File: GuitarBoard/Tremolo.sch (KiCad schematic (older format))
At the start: 37 parts, among them Q2 2N5088, Q7 2N5088, Q8 2N5088, Q9 2N5088

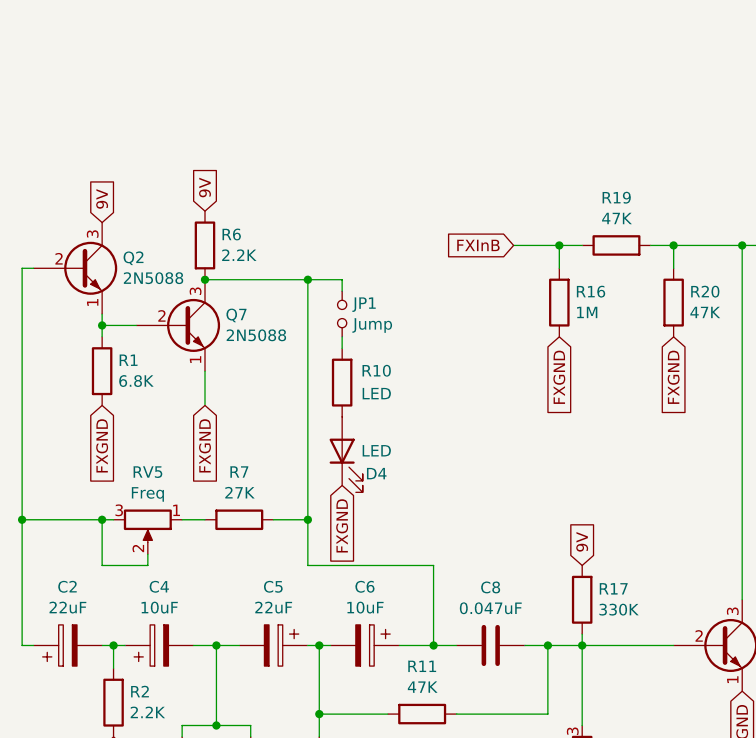
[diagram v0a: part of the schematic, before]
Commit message: Finished placing components. Adding traces right now
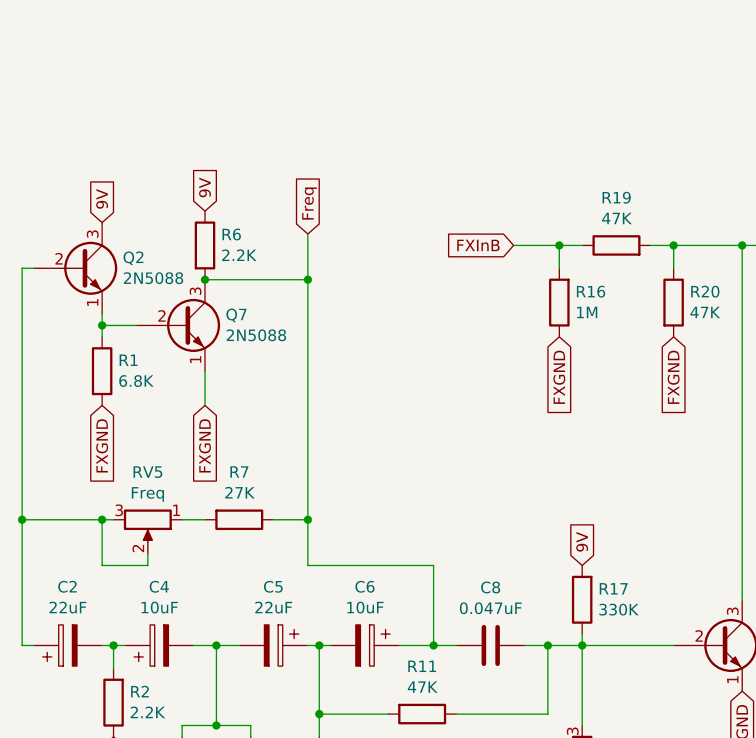
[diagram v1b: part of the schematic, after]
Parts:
- removed D4: LED, LED_THT:LED_D5.0mm, symbol Device:LED
- removed JP1: Jump, Connector_PinSocket_2.54mm:PinSocket_1x02_P2.54mm_Vertical, symbol Device:Jumper_NO_Small
- removed R10: LED, Resistor_THT:R_Axial_DIN0207_L6.3mm_D2.5mm_P10.16mm_Horizontal, symbol Device:R
- C10, C9: footprint (none) -> libraries:CP_Radial_D5.0mm_P2.00mm
- C2, C4, C5, C6: footprint (none) -> libraries:CP_Radial_D6.3mm_P2.50mm
- RV5, RV6: footprint Potentiometer_THT:Potentiometer_Bourns_3386F_Vertical -> Connector_PinSocket_2.54mm:PinSocket_1x03_P2.54mm_Vertical
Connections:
- net Freq: now reaches C6.1, C8.2, Q7.3 (C), R6.2, R7.1
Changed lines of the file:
@@
 F 0 "RV5" V 2043 3950 50  0000 C CNN
 F 1 "Freq" V 2134 3950 50  0000 C CNN
-F 2 "Potentiometer_THT:Potentiometer_Bourns_3386F_Vertical" H 2250 3950 50  0001 C CNN
+F 2 "Connector_PinSocket_2.54mm:PinSocket_1x03_P2.54mm_Vertical" H 2250 3950 50  0001 C CNN
 F 3 "~" H 2250 3950 50  0001 C CNN
 	1    2250 3950
@@
 	2950 3950 2800 3950
 Connection ~ 2500 2900
-$Comp
-L Device:R R10
-U 1 1 60E2EF4D
-P 3100 3350
-F 0 "R10" H 2950 3300 50  0000 C CNN
-F 1 "LED" H 2950 3400 50  0000 C CNN
-F 2 "Resistor_THT:R_Axial_DIN0207_L6.3mm_D2.5mm_P10.16mm_Horizontal" V 3030 3350 50  0001 C CNN
-F 3 "~" H 3100 3350 50  0001 C CNN
-	1    3100 3350
-	-1   0    0    1
-$EndComp
 Connection ~ 2950 2900
-$Comp
-L Device:LED D4
-U 1 1 60E2FC8E
-P 3100 3650
-F 0 "D4" V 3000 3500 50  0000 C CNN
-F 1 "LED" V 3100 3500 50  0000 C CNN
-F 2 "LED_THT:LED_D5.0mm" H 3100 3650 50  0001 C CNN
-F 3 "~" H 3100 3650 50  0001 C CNN
-	1    3100 3650
-	0    -1   -1   0
-$EndComp
-Wire Wire Line
-	3100 2950 3100 2900
-Wire Wire Line
-	2950 2900 3100 2900
 $Comp
 L Device:CP C2
@@
 F 0 "C2" V 2155 4500 50  0000 C CNN
 F 1 "22uF" V 2064 4500 50  0000 C CNN
-F 2 "" H 1938 4350 50  0001 C CNN
+F 2 "libraries:CP_Radial_D6.3mm_P2.50mm" H 1938 4350 50  0001 C CNN
 F 3 "~" H 1900 4500 50  0001 C CNN
 	1    1900 4500
@@
 F 0 "C4" V 2555 4500 50  0000 C CNN
 F 1 "10uF" V 2464 4500 50  0000 C CNN
-F 2 "" H 2338 4350 50  0001 C CNN
+F 2 "libraries:CP_Radial_D6.3mm_P2.50mm" H 2338 4350 50  0001 C CNN
 F 3 "~" H 2300 4500 50  0001 C CNN
 	1    2300 4500
@@
 F 0 "C5" V 2545 4500 50  0000 C CNN
 F 1 "22uF" V 2636 4500 50  0000 C CNN
-F 2 "" H 2838 4350 50  0001 C CNN
+F 2 "libraries:CP_Radial_D6.3mm_P2.50mm" H 2838 4350 50  0001 C CNN
 F 3 "~" H 2800 4500 50  0001 C CNN
 	1    2800 4500
@@
 F 0 "C6" V 2945 4500 50  0000 C CNN
 F 1 "10uF" V 3036 4500 50  0000 C CNN
-F 2 "" H 3238 4350 50  0001 C CNN
+F 2 "libraries:CP_Radial_D6.3mm_P2.50mm" H 3238 4350 50  0001 C CNN
 F 3 "~" H 3200 4500 50  0001 C CNN
 	1    3200 4500
@@
 	3000 4800 3000 4500
 Wire Wire Line
-	3100 3200 3100 3150
-$Comp
-L Device:Jumper_NO_Small JP1
-U 1 1 60E45440
-P 3100 3050
-F 0 "JP1" V 3054 3098 50  0000 L CNN
-F 1 "Jump" V 3145 3098 50  0000 L CNN
-F 2 "Connector_PinSocket_2.54mm:PinSocket_1x02_P2.54mm_Vertical" H 3100 3050 50  0001 C CNN
-F 3 "~" H 3100 3050 50  0001 C CNN
-	1    3100 3050
-	0    1    1    0
-$EndComp
-Wire Wire Line
 	2950 3950 2950 4150
 Connection ~ 2950 3950
@@
 Text GLabel 2500 3450 3    50   Input ~ 0
 FXGND
-Text GLabel 3100 3800 3    50   Input ~ 0
-FXGND
 Wire Wire Line
 	4000 4500 4150 4500
@@
 F 0 "RV6" H 4080 4954 50  0000 R CNN
 F 1 "Amp" H 4080 5045 50  0000 R CNN
-F 2 "Potentiometer_THT:Potentiometer_Bourns_3386F_Vertical" H 4150 5000 50  0001 C CNN
+F 2 "Connector_PinSocket_2.54mm:PinSocket_1x03_P2.54mm_Vertical" H 4150 5000 50  0001 C CNN
 F 3 "~" H 4150 5000 50  0001 C CNN
 	1    4150 5000
@@
 F 0 "C9" V 4845 2750 50  0000 C CNN
 F 1 "4.7uF" V 4936 2750 50  0000 C CNN
-F 2 "" H 5138 2600 50  0001 C CNN
+F 2 "libraries:CP_Radial_D5.0mm_P2.00mm" H 5138 2600 50  0001 C CNN
 F 3 "~" H 5100 2750 50  0001 C CNN
 	1    5100 2750
@@
 F 0 "C10" V 6205 2400 50  0000 C CNN
 F 1 "4.7uF" V 6114 2400 50  0000 C CNN
-F 2 "" H 5988 2250 50  0001 C CNN
+F 2 "libraries:CP_Radial_D5.0mm_P2.00mm" H 5988 2250 50  0001 C CNN
 F 3 "~" H 5950 2400 50  0001 C CNN
 	1    5950 2400
@@
 Text GLabel 6000 4350 1    50   Input ~ 0
 9V
+Text GLabel 2950 2700 1    50   Input ~ 0
+Freq
+Wire Wire Line
+	2950 2700 2950 2900
 $EndSCHEMATC
